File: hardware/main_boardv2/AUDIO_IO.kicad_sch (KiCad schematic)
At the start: 22 parts, among them IC501 PCM1780DBQR, IC502 LM321LVIDBVR, IC503 LM321LVIDBVR, J501 Conn_01x03_Pin, J502 trs_audio_jack

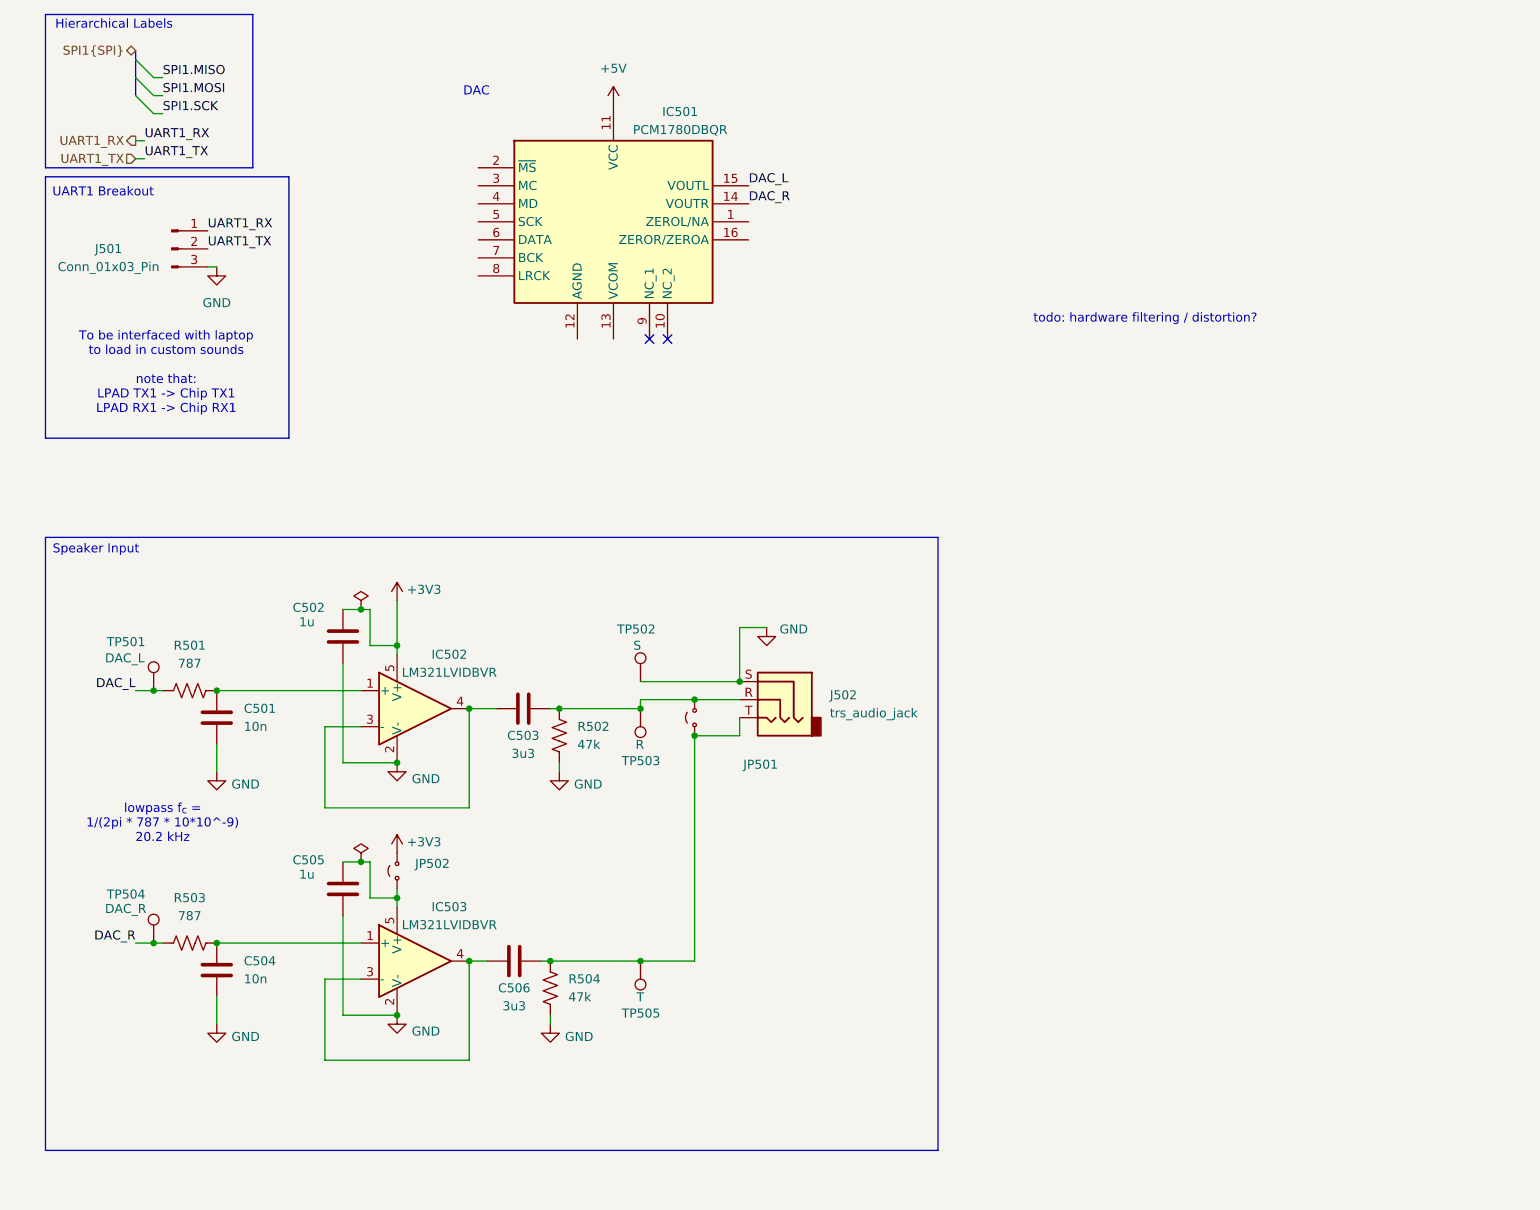
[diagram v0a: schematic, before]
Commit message: dubious hardware schematic 'done'. need to go back and revise passives and verify IC connections, esp the DAC. modified readme
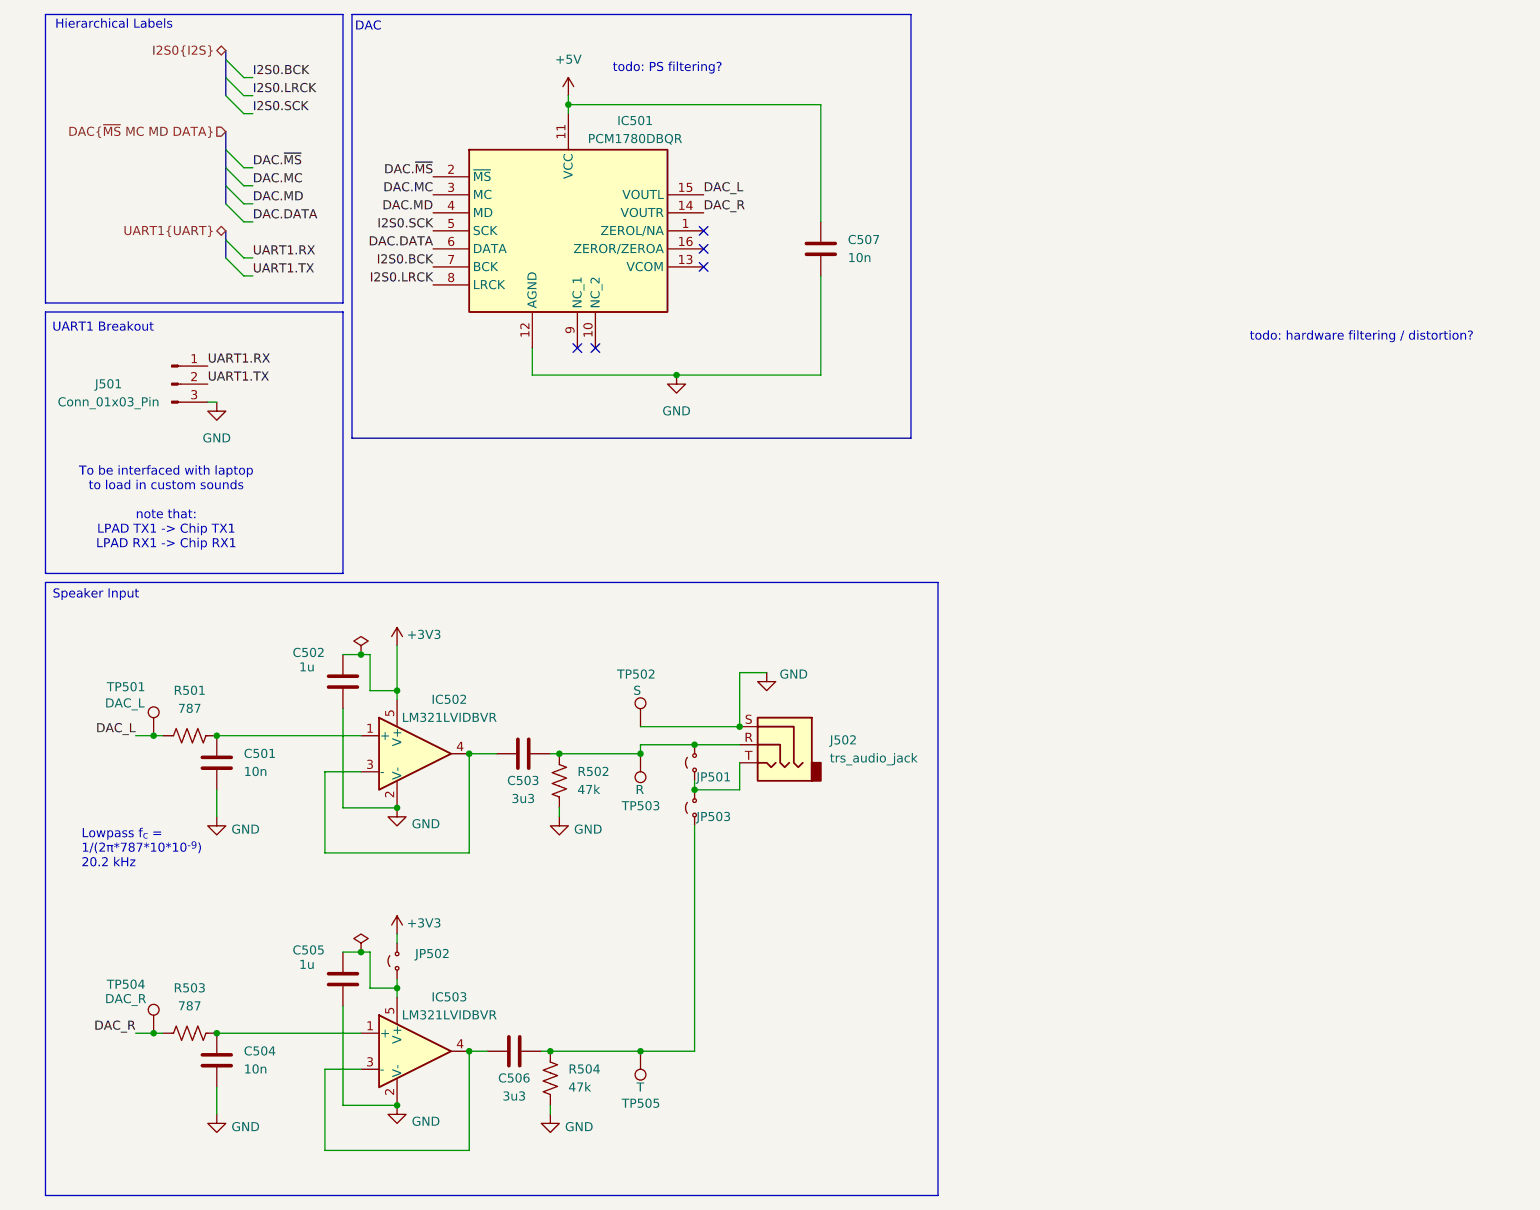
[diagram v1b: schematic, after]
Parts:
- added C507: 10n, Capacitor_SMD:C_0805_2012Metric, symbol ECE445L:C
- added JP503: Jumper_2_Small_Open, Jumper:SolderJumper-2_P1.3mm_Open_RoundedPad1.0x1.5mm, symbol Jumper:Jumper_2_Small_Open
- IC501: footprint SOP64P600X175-16N -> SamacSys_Parts:SOP64P600X175-16N
- J502: footprint (none) -> 445L:Jack_3.5mm_CUI_SJ1-3523N_Horizontal
- JP501, JP502: footprint (none) -> Jumper:SolderJumper-2_P1.3mm_Open_RoundedPad1.0x1.5mm
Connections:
- net +5V: now also C507.2
- net GND: now also IC501.12 (AGND), C507.1
- net at C506.1, R504.2, TP505.1: now also JP503.1 (A); no longer J502.T, JP501.1 (A)
- net DAC.~{MS}: now reaches IC501.2 (~{MS})
- net DAC.MC: now reaches IC501.3 (MC)
- net DAC.MD: now reaches IC501.4 (MD)
- net I2S0.SCK: now reaches IC501.5 (SCK)
- net DAC.DATA: now reaches IC501.6 (DATA)
- net I2S0.BCK: now reaches IC501.7 (BCK)
- net I2S0.LRCK: now reaches IC501.8 (LRCK)
- net UART1_RX renamed UART1.RX
- net UART1_TX renamed UART1.TX
- new net: J502.T, JP501.1 (A), JP503.2 (B)
- no-connect marks 2 -> 5
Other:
- note added: "Lowpass f_{c} = 1/(2π*787*10*10^{-9}) 20.2 kHz"
- note added: "todo: PS filtering?"
- note removed: "lowpass f_{c} = 1/(2pi * 787 * 10*10^-9) 20.2 kHz"
- moved on the sheet: C501, C502, C503, C504, C505, C506, IC501, IC502, IC503, J501, J502, JP501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

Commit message: schematic sorta done? resized all RC packages to 0805
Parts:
- added J503: 2x5 Socket Pins, SamacSys_Parts:logic_analyzer_slot_2x5_2.54mm, symbol SamacSys_Parts:Conn_02x05_Even_Odd
- C507: value 10n -> 0u1
- renumbered C504 to C502, C502 to C503, C505 to C504, C506 to C505, C503 to C506, IC502 to IC501, IC503 to IC502, IC501 to IC503, JP502 to JP501, JP501 to JP502, R503 to R502, R504 to R503, R502 to R504, TP504 to TP502, TP502 to TP503, TP503 to TP504
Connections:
- net DAC.DATA: now also J503.6 (Pin_6)
- net DAC.MC: now also J503.1 (Pin_1)
- net DAC.MD: now also J503.4 (Pin_4)
- net DAC.~{MS}: now also J503.2 (Pin_2)
- net GND: now also J503.9 (Pin_9)
- net I2S0.BCK: now also J503.5 (Pin_5)
- net I2S0.LRCK: now also J503.8 (Pin_8)
- net I2S0.SCK: now also J503.3 (Pin_3)
- no-connect marks 5 -> 7
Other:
- note added: "Chn 0 - DAC.~{MS} Chn 1 - DAC.MC Chn 2 - DAC.MD Chn 3 - I2S0.SCK Chn 4 - DAC.DATA Chn 5 - I2S0.BCK Chn 6 - I2S0.LRCK Chn 7 - N/C"
- note added: "I2S Logic Analyzer Breakout"
- note added: "Short JP501 and open JP503 to have mono audio"
- note added: "To be interfaced with laptop to load in custom sounds"
- note removed: "To be interfaced with laptop to load in custom sounds note that: LPAD TX1 -> Chip TX1 LPAD RX1 -> Chip RX1"
- moved on the sheet: JP503

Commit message: resized all package to 0603
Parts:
- C501, C502, C503, C504, C507: footprint Capacitor_SMD:C_0805_2012Metric -> Capacitor_SMD:C_0603_1608Metric; Mouser Price/Stock https://www.mouser.com/ProductDetail/Samsung-Electro-Mechan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 -> (none)
- C505, C506: footprint Capacitor_SMD:C_0805_2012Metric -> Capacitor_SMD:C_0603_1608Metric; Mouser Price/Stock https://www.mouser.com/ProductDetail/TDK/C2012X7R1V335K125A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 -> (none)
- R501, R502: footprint Resistor_SMD:R_0805_2012Metric -> Resistor_SMD:R_0603_1608Metric; Mouser Price/Stock https://www.mouser.com/ProductDetail/Vishay/CRCW0805787RFKE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 -> (none)
- R503, R504: footprint Resistor_SMD:R_0805_2012Metric -> Resistor_SMD:R_0603_1608Metric; Mouser Price/Stock https://www.mouser.com/ProductDetail/YAGEO/RC0805JR-7W47KL?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 -> (none)
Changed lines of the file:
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@@
 			)
 		)
-		(property "Footprint" "Resistor_SMD:R_0805_2012Metric"
+		(property "Footprint" "Resistor_SMD:R_0603_1608Metric"
 			(at 88.138 121.92 90)
 			(effects
@@
 			)
 		)
-		(property "Mouser Price/Stock" "https://www.mouser.com/ProductDetail/YAGEO/RC0805JR-7W47KL?qs=tggtontpCXNoMeTIW8%252BKHA%3D%3D"
+		(property "Mouser Price/Stock" ""
 			(at 86.36 121.92 0)
 			(effects
@@
 			)
 		)
-		(property "Footprint" "Capacitor_SMD:C_0805_2012Metric"
+		(property "Footprint" "Capacitor_SMD:C_0603_1608Metric"
 			(at 56.8452 153.67 0)
 			(effects
@@
 			)
 		)
-		(property "Mouser Price/Stock" "https://www.mouser.com/ProductDetail/Samsung-Electro-Mechanics/CL21B105KPFNNNE?qs=349EhDEZ59rb3V94UrmRdQ%3D%3D"
+		(property "Mouser Price/Stock" ""
 			(at 55.88 149.86 0)
 			(effects
@@
 			)
 		)
-		(property "Footprint" "Capacitor_SMD:C_0805_2012Metric"
+		(property "Footprint" "Capacitor_SMD:C_0603_1608Metric"
 			(at 37.1348 115.57 0)
 			(effects
@@
 			)
 		)
-		(property "Mouser Price/Stock" "https://www.mouser.com/ProductDetail/Samsung-Electro-Mechanics/CL21A106KPFNNNE?qs=sGAEpiMZZMt7gvpyg0xT8jBAVP%252BdkPhuUJvUBe19zr8%3D"
+		(property "Mouser Price/Stock" ""
 			(at 38.1 119.38 0)
 			(effects
@@
 			)
 		)
-		(property "Footprint" "Resistor_SMD:R_0805_2012Metric"
+		(property "Footprint" "Resistor_SMD:R_0603_1608Metric"
 			(at 86.868 163.83 90)
 			(effects
@@
 			)
 		)
-		(property "Mouser Price/Stock" "https://www.mouser.com/ProductDetail/YAGEO/RC0805JR-7W47KL?qs=tggtontpCXNoMeTIW8%252BKHA%3D%3D"
+		(property "Mouser Price/Stock" ""
 			(at 85.09 163.83 0)
 			(effects
@@
 			)
 		)
-		(property "Footprint" "Capacitor_SMD:C_0805_2012Metric"
+		(property "Footprint" "Capacitor_SMD:C_0603_1608Metric"
 			(at 76.2 160.9852 0)
 			(effects
@@
 			)
 		)
-		(property "Mouser Price/Stock" "https://www.mouser.com/ProductDetail/TDK/C2012X7R1V335K125AC?qs=U4gclJHtfSj5XsYUBUaOrg%3D%3D"
+		(property "Mouser Price/Stock" ""
 			(at 80.01 160.02 90)
 			(effects
@@
 			)
 		)
-		(property "Footprint" "Capacitor_SMD:C_0805_2012Metric"
+		(property "Footprint" "Capacitor_SMD:C_0603_1608Metric"
 			(at 37.1348 157.48 0)
 			(effects
@@
 			)
 		)
-		(property "Mouser Price/Stock" "https://www.mouser.com/ProductDetail/Samsung-Electro-Mechanics/CL21A106KPFNNNE?qs=sGAEpiMZZMt7gvpyg0xT8jBAVP%252BdkPhuUJvUBe19zr8%3D"
+		(property "Mouser Price/Stock" ""
 			(at 38.1 161.29 0)
 			(effects
@@
 			)
 		)
-		(property "Footprint" "Capacitor_SMD:C_0805_2012Metric"
+		(property "Footprint" "Capacitor_SMD:C_0603_1608Metric"
 			(at 56.8452 111.76 0)
 			(effects
@@
 			)
 		)
-		(property "Mouser Price/Stock" "https://www.mouser.com/ProductDetail/Samsung-Electro-Mechanics/CL21B105KPFNNNE?qs=349EhDEZ59rb3V94UrmRdQ%3D%3D"
+		(property "Mouser Price/Stock" ""
 			(at 55.88 107.95 0)
 			(effects
@@
 			)
 		)
-		(property "Footprint" "Capacitor_SMD:C_0805_2012Metric"
+		(property "Footprint" "Capacitor_SMD:C_0603_1608Metric"
 			(at 122.2248 43.18 0)
 			(effects
@@
 			)
 		)
-		(property "Mouser Price/Stock" "https://www.mouser.com/ProductDetail/Samsung-Electro-Mechanics/CL21A106KPFNNNE?qs=sGAEpiMZZMt7gvpyg0xT8jBAVP%252BdkPhuUJvUBe19zr8%3D"
+		(property "Mouser Price/Stock" ""
 			(at 123.19 46.99 0)
 			(effects
@@
 			)
 		)
-		(property "Footprint" "Capacitor_SMD:C_0805_2012Metric"
+		(property "Footprint" "Capacitor_SMD:C_0603_1608Metric"
 			(at 77.47 119.0752 0)
 			(effects
@@
 			)
 		)
-		(property "Mouser Price/Stock" "https://www.mouser.com/ProductDetail/TDK/C2012X7R1V335K125AC?qs=U4gclJHtfSj5XsYUBUaOrg%3D%3D"
+		(property "Mouser Price/Stock" ""
 			(at 81.28 118.11 90)
 			(effects
@@
 			)
 		)
-		(property "Footprint" "Resistor_SMD:R_0805_2012Metric"
+		(property "Footprint" "Resistor_SMD:R_0603_1608Metric"
 			(at 34.29 159.258 90)
 			(effects
@@
 			)
 		)
-		(property "Mouser Price/Stock" "https://www.mouser.com/ProductDetail/Vishay/CRCW0805787RFKEA?qs=Lu3mkJd%252BoBHFo%2FQlWc6ASQ%3D%3D"
+		(property "Mouser Price/Stock" ""
 			(at 34.29 157.48 90)
 			(effects
@@
 			)
 		)
-		(property "Footprint" "Resistor_SMD:R_0805_2012Metric"
+		(property "Footprint" "Resistor_SMD:R_0603_1608Metric"
 			(at 34.29 117.348 90)
 			(effects
@@
 			)
 		)
-		(property "Mouser Price/Stock" "https://www.mouser.com/ProductDetail/Vishay/CRCW0805787RFKEA?qs=Lu3mkJd%252BoBHFo%2FQlWc6ASQ%3D%3D"
+		(property "Mouser Price/Stock" ""
 			(at 34.29 115.57 90)
 			(effects
